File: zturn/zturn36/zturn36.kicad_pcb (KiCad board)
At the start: 4 copper layers, 189.9 x 136.5 mm, 63 parts, among them J11 Conn_02x40_Odd_Even, J12 Conn_02x40_Odd_Even, J5V1 Conn_01x03, Q1 SSM6N15AFU, Q2 SSM6N15AFU, Q3 SSM6N15AFU, Q4 SSM6N15AFU, Q5 SSM6N15AFU, Q6 SSM6N15AFU, Q7 SSM6N15AFU, Q8 SSM6N15AFU, Q9 SSM6N15AFU, U1 74AXP4T245, U10 74AXP4T245, U11 74AXP4T245, U12 74AXP4T245, U13 74AXP4T245, U2 74AXP4T245, U3 74AXP4T245, U8 74AXP4T245, U9 74AXP4T245

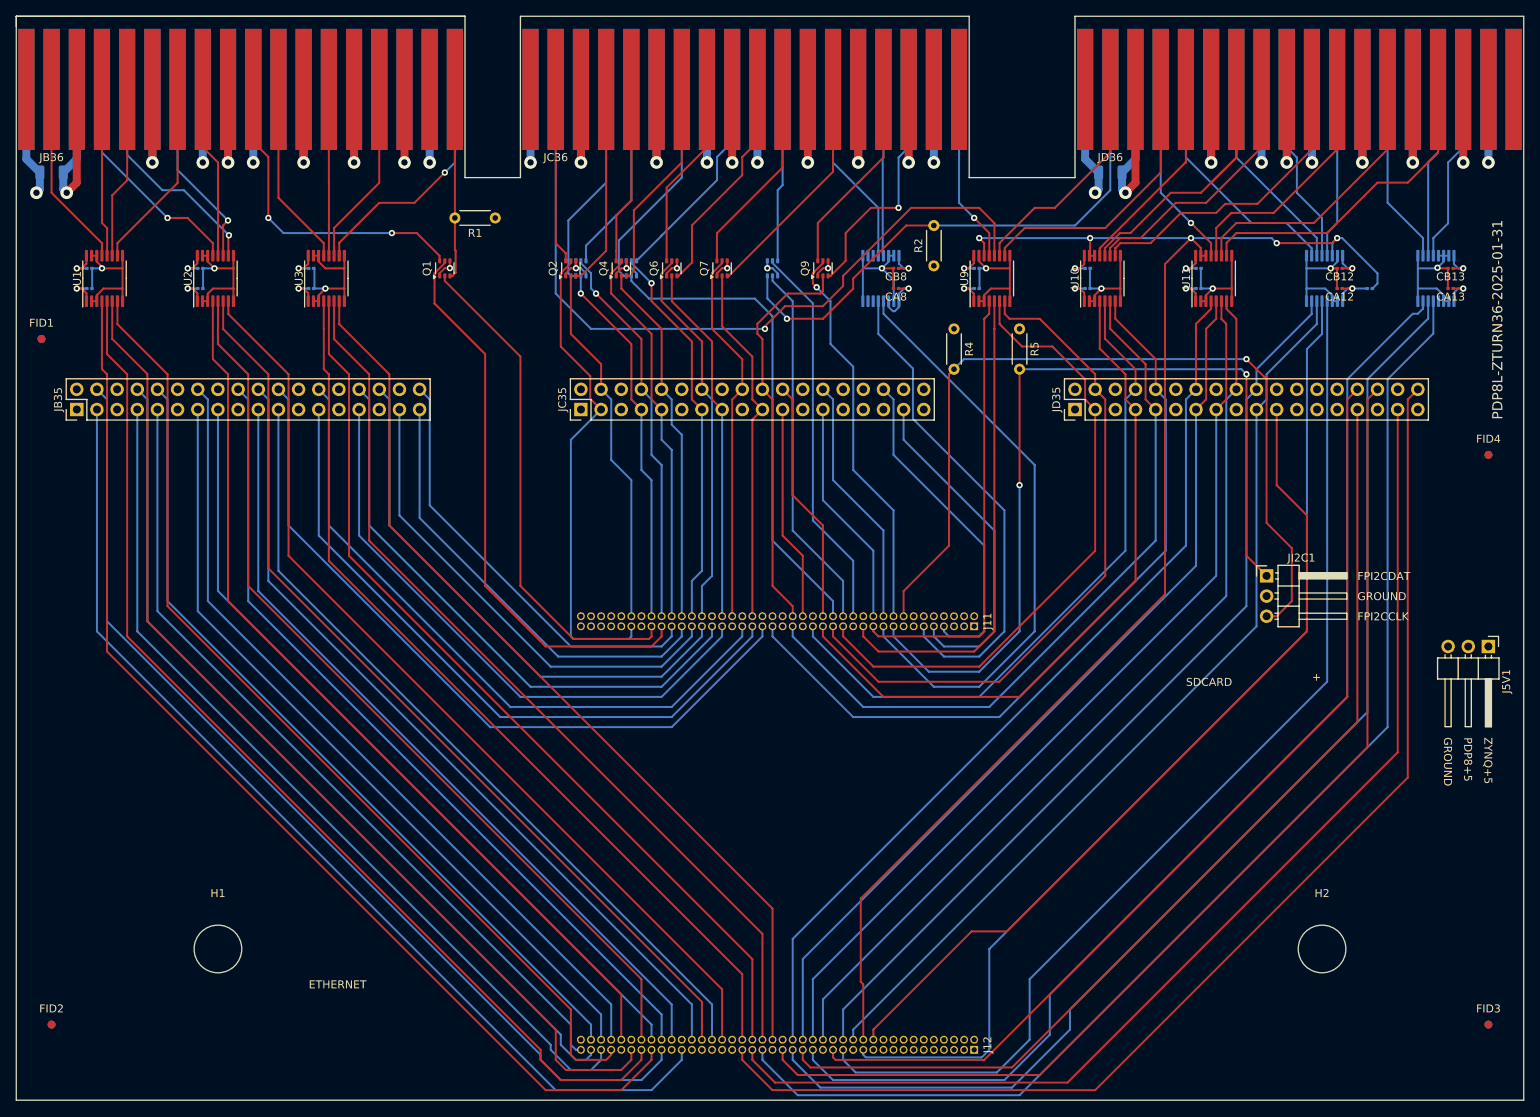
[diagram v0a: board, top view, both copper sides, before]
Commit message: put 2024-12-30 version of zturn35,36 boards back
the 2024-12-30 design had 5V I2C bus via 74AXP245s
the newer boards had 3.3V I2C bus directly on FPGA

the old boards work perfectly fine so go back to them
...rather than make new boards
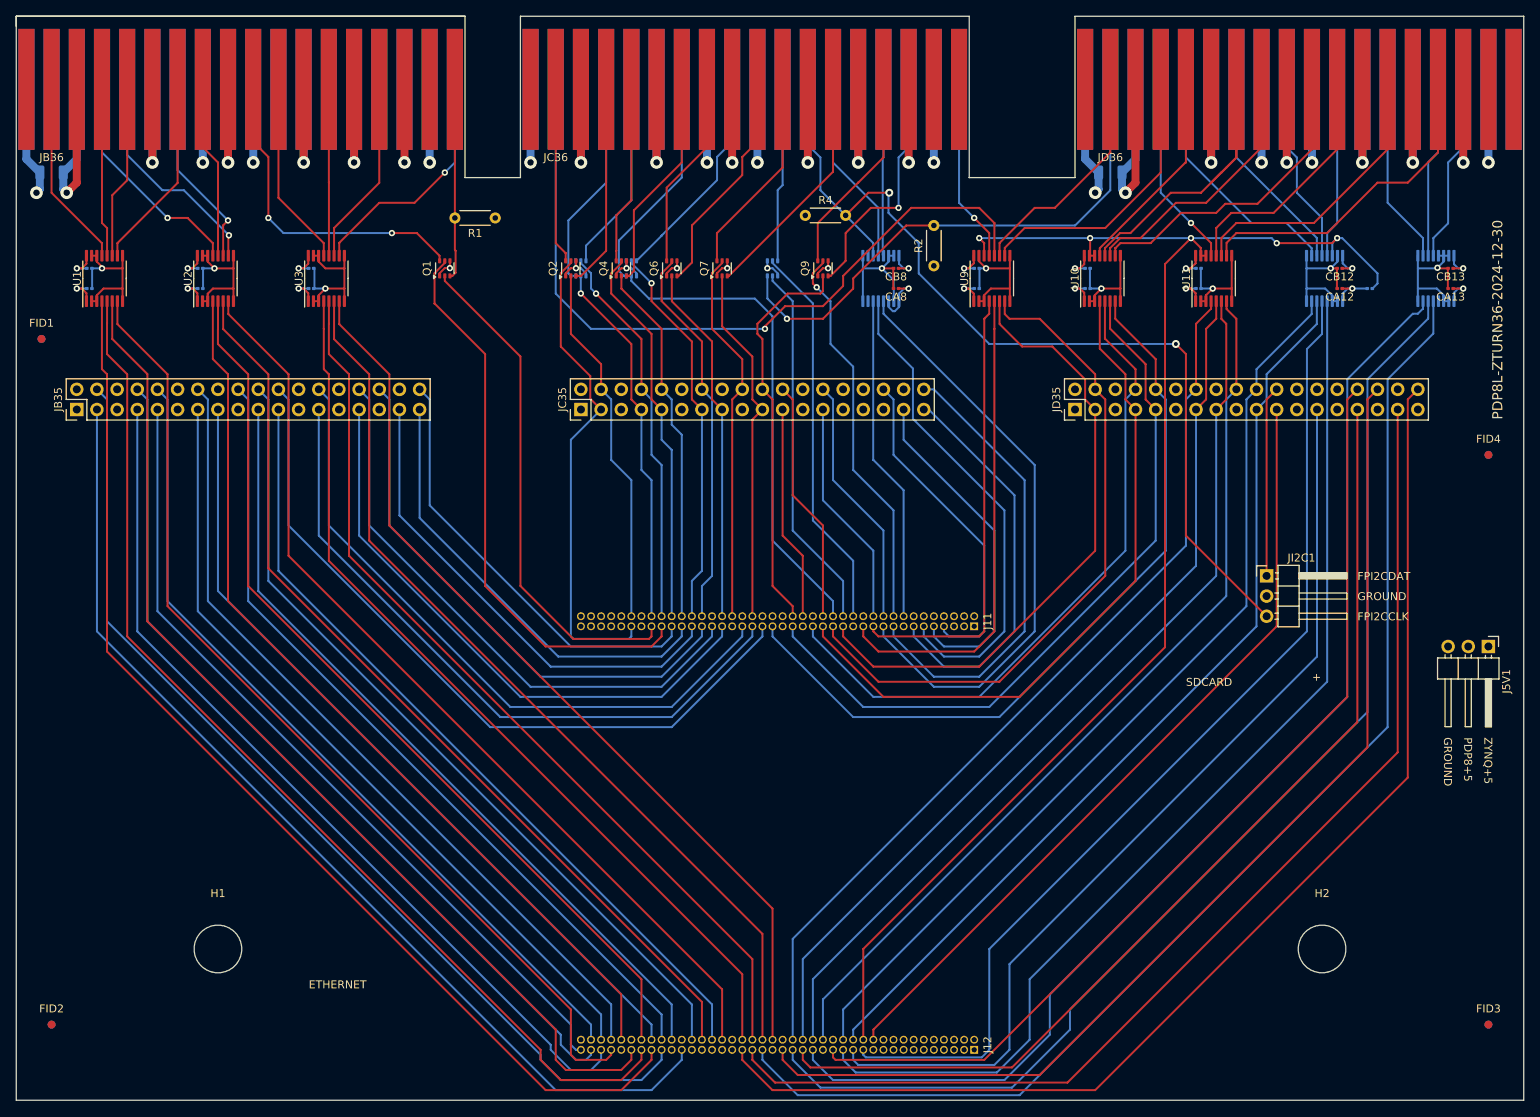
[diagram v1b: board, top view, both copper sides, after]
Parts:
- removed R5: 2.2K, Resistor_THT:R_Axial_DIN0204_L3.6mm_D1.6mm_P5.08mm_Horizontal
- R4: value 2.2K -> 1K
- moved R4 23.6 mm to (99.4, 25.1), turned to 0 degrees
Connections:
- net /iMEMINCR renamed /i_MEMINCR
- J11 pad 13: unconnected-(J11-Pin_13-Pad13) -> /FPI2CDDIR
- J11 pad 17: /FPI2CDAT -> /FPI2CDATA
- J12 pad 25: unconnected-(J12-Pin_25-Pad25) -> /FPI2CDENA
- JC35 pad 35: unconnected-(JC35-Pin_35-Pad35) -> /FPI2CDDIR
- JC35 pad 36: unconnected-(JC35-Pin_36-Pad36) -> /FPI2CDATA
- JC36 pad N2: unconnected-(JC36-PadN2) -> /EPI2CCLK
- JD35 pad 22: unconnected-(JD35-Pin_22-Pad22) -> /EPI2CDAT
- JD35 pad 25: unconnected-(JD35-Pin_25-Pad25) -> /FPI2CDENA
- JI2C1 pad 1: /FPI2CDAT -> /EPI2CDAT
- JI2C1 pad 3: /FPI2CCLK -> /EPI2CCLK
- R4 pad 1: +3V3 -> +5V
- R4 pad 2: /FPI2CCLK -> /EPI2CCLK
- U8 pad 11: unconnected-(U8-2B1-Pad11) -> /EPI2CCLK
- U8 pad 6: unconnected-(U8-2A1-Pad6) -> /FPI2CCLK
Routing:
- net /FPI2CDENA: track 0.00 -> 118.7 mm
- net /EPI2CCLK: track 0.00 -> 110.9 mm, vias 0 -> 2
- net /FPI2CDAT: track 108.8 -> 0.00 mm, vias 2 -> 0
- net /FPI2CCLK: track 108.1 -> 41.3 mm, vias 1 -> 0
- net /FPI2CDATA: track 0.00 -> 58.7 mm
- net /FPI2CDDIR: track 0.00 -> 49.8 mm
- net /EPI2CDAT: track 0.00 -> 24.0 mm
- net /x_INPUTBUS: track 106.2 -> 100.4 mm
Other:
- board text added: "PDP8L-ZTURN36-2024-12-30"
- board text removed: "PDP8L-ZTURN36-2025-01-31"
